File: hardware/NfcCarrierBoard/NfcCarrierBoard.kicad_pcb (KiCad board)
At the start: 2 copper layers, 80 x 100 mm, 50 parts, among them J1 Barrel_Jack, J2 Conn_01x03, J3 JST SH 4, J4 Grove, J5 Conn_01x03, J6 UART, J7 Grove UART, Q1 NMOS, Q2 NMOS, SW1 RESET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

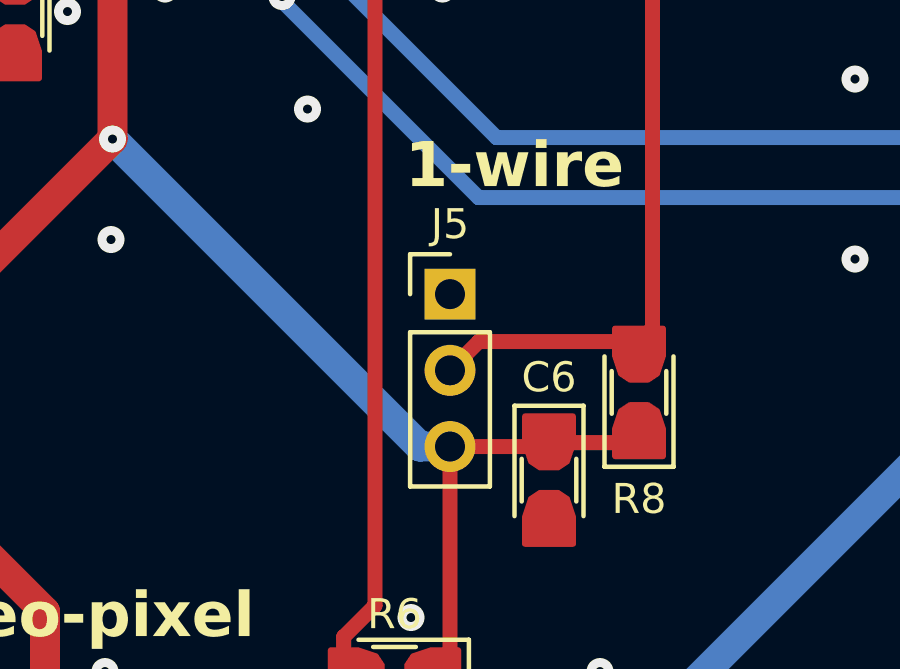
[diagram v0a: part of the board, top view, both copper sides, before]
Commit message: Change footprint for 1-wire header Not an electrical/physical board change, but this makes 3D renders show the proper connector
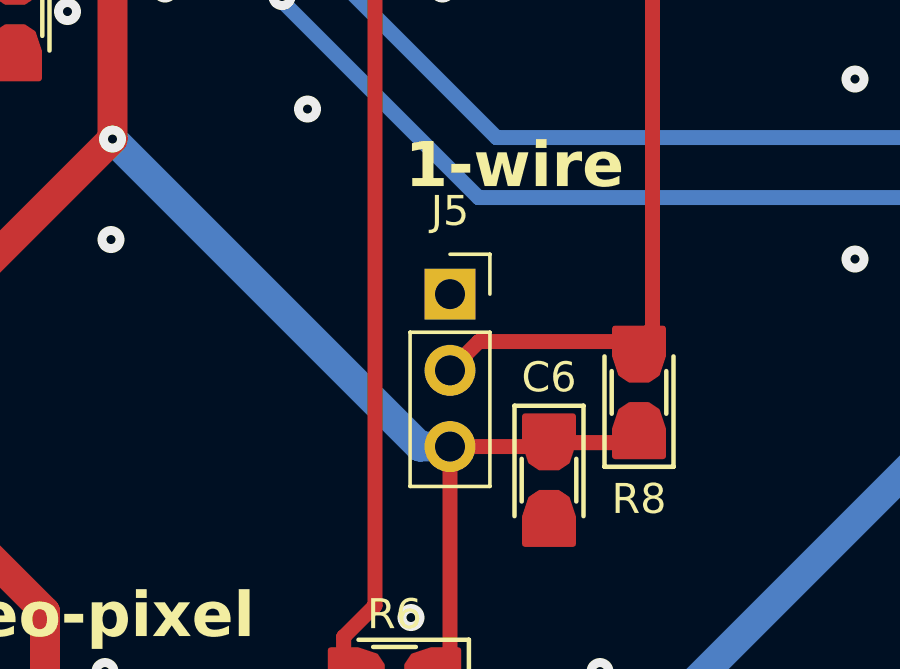
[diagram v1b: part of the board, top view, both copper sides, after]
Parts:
- J5: footprint Connector_PinHeader_2.54mm:PinHeader_1x03_P2.54mm_Vertical -> Connector_PinSocket_2.54mm:PinSocket_1x03_P2.54mm_Vertical
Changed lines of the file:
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@@
 		(sheetname "Root")
 		(sheetfile "NfcCarrierBoard.kicad_sch")
-		(attr through_hole dnp)
+		(attr through_hole)
 		(fp_line
 			(start -1.33 -1.33)
@@
 		)
 	)
-	(footprint "Connector_PinHeader_2.54mm:PinHeader_1x03_P2.54mm_Vertical"
+	(footprint "Connector_PinSocket_2.54mm:PinSocket_1x03_P2.54mm_Vertical"
 		(layer "F.Cu")
 		(at 135.5 126.42)
-		(descr "Through hole straight pin header, 1x03, 2.54mm pitch, single row")
-		(tags "Through hole pin header THT 1x03 2.54mm single row")
+		(descr "Through hole straight socket strip, 1x03, 2.54mm pitch, single row (from Kicad 4.0.7), script generated")
+		(tags "Through hole socket strip THT 1x03 2.54mm single row")
 		(property "Reference" "J5"
-			(at 0 -2.33 0)
-			(unlocked yes)
+			(at 0 -2.77 0)
 			(layer "F.SilkS")
 			(effects
@@
 		)
 		(property "Value" "Conn_01x03"
-			(at 0 7.41 0)
+			(at 0 7.85 0)
 			(layer "F.Fab")
 			(effects
@@
 			)
 		)
-		(property "Footprint" "Connector_PinHeader_2.54mm:PinHeader_1x03_P2.54mm_Vertical"
+		(property "Footprint" "Connector_PinSocket_2.54mm:PinSocket_1x03_P2.54mm_Vertical"
 			(at 0 0 0)
 			(unlocked yes)
@@
 		(attr through_hole)
 		(fp_line
-			(start -1.33 -1.33)
-			(end 0 -1.33)
+			(start -1.33 1.27)
+			(end -1.33 6.41)
 			(stroke
-				(width 0.15)
+				(width 0.12)
 				(type solid)
 			)
@@
 		)
 		(fp_line
-			(start -1.33 0)
-			(end -1.33 -1.33)
+			(start -1.33 1.27)
+			(end 1.33 1.27)
 			(stroke
-				(width 0.15)
+				(width 0.12)
 				(type solid)
 			)
@@
 		)
 		(fp_line
-			(start -1.33 1.27)
-			(end -1.33 6.41)
+			(start -1.33 6.41)
+			(end 1.33 6.41)
 			(stroke
-				(width 0.15)
+				(width 0.12)
 				(type solid)
 			)
@@
 		)
 		(fp_line
-			(start -1.33 1.27)
-			(end 1.33 1.27)
+			(start 0 -1.33)
+			(end 1.33 -1.33)
 			(stroke
-				(width 0.15)
+				(width 0.12)
 				(type solid)
 			)
@@
 		)
 		(fp_line
-			(start -1.33 6.41)
-			(end 1.33 6.41)
+			(start 1.33 -1.33)
+			(end 1.33 0)
 			(stroke
-				(width 0.15)
+				(width 0.12)
 				(type solid)
 			)
@@
 			(end 1.33 6.41)
 			(stroke
-				(width 0.15)
+				(width 0.12)
 				(type solid)
 			)
@@
 		(fp_line
 			(start -1.8 -1.8)
-			(end -1.8 6.85)
+			(end 1.75 -1.8)
 			(stroke
 				(width 0.05)
@@
 		(fp_line
 			(start -1.8 6.85)
-			(end 1.8 6.85)
+			(end -1.8 -1.8)
 			(stroke
 				(width 0.05)
@@
 		)
 		(fp_line
-			(start 1.8 -1.8)
-			(end -1.8 -1.8)
+			(start 1.75 -1.8)
+			(end 1.75 6.85)
 			(stroke
 				(width 0.05)
@@
 		)
 		(fp_line
-			(start 1.8 6.85)
-			(end 1.8 -1.8)
+			(start 1.75 6.85)
+			(end -1.8 6.85)
 			(stroke
 				(width 0.05)
@@
 		)
 		(fp_line
-			(start -1.27 -0.635)
-			(end -0.635 -1.27)
+			(start -1.27 -1.27)
+			(end 0.635 -1.27)
 			(stroke
 				(width 0.1)
@@
 		(fp_line
 			(start -1.27 6.35)
-			(end -1.27 -0.635)
+			(end -1.27 -1.27)
 			(stroke
 				(width 0.1)
@@
 		)
 		(fp_line
-			(start -0.635 -1.27)
-			(end 1.27 -1.27)
+			(start 0.635 -1.27)
+			(end 1.27 -0.635)
 			(stroke
 				(width 0.1)
@@
 		)
 		(fp_line
-			(start 1.27 -1.27)
+			(start 1.27 -0.635)
 			(end 1.27 6.35)
 			(stroke
@@
 			(pintype "passive")
 		)
-		(model "${KICAD8_3DMODEL_DIR}/Connector_PinHeader_2.54mm.3dshapes/PinHeader_1x03_P2.54mm_Vertical.wrl"
+		(model "${KICAD8_3DMODEL_DIR}/Connector_PinSocket_2.54mm.3dshapes/PinSocket_1x03_P2.54mm_Vertical.wrl"
 			(offset
 				(xyz 0 0 0)
